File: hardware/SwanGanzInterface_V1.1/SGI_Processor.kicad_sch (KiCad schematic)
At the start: 29 parts, among them J2 Conn_01x08_Pin, SW2 MODE, SW3 ENTER, SW4 MODE, U4 XM0G3507QPTRQ1, U5 AdaFruit_1590, Y1 ABM8AIG-40.000MHZ-12-2Z-T3

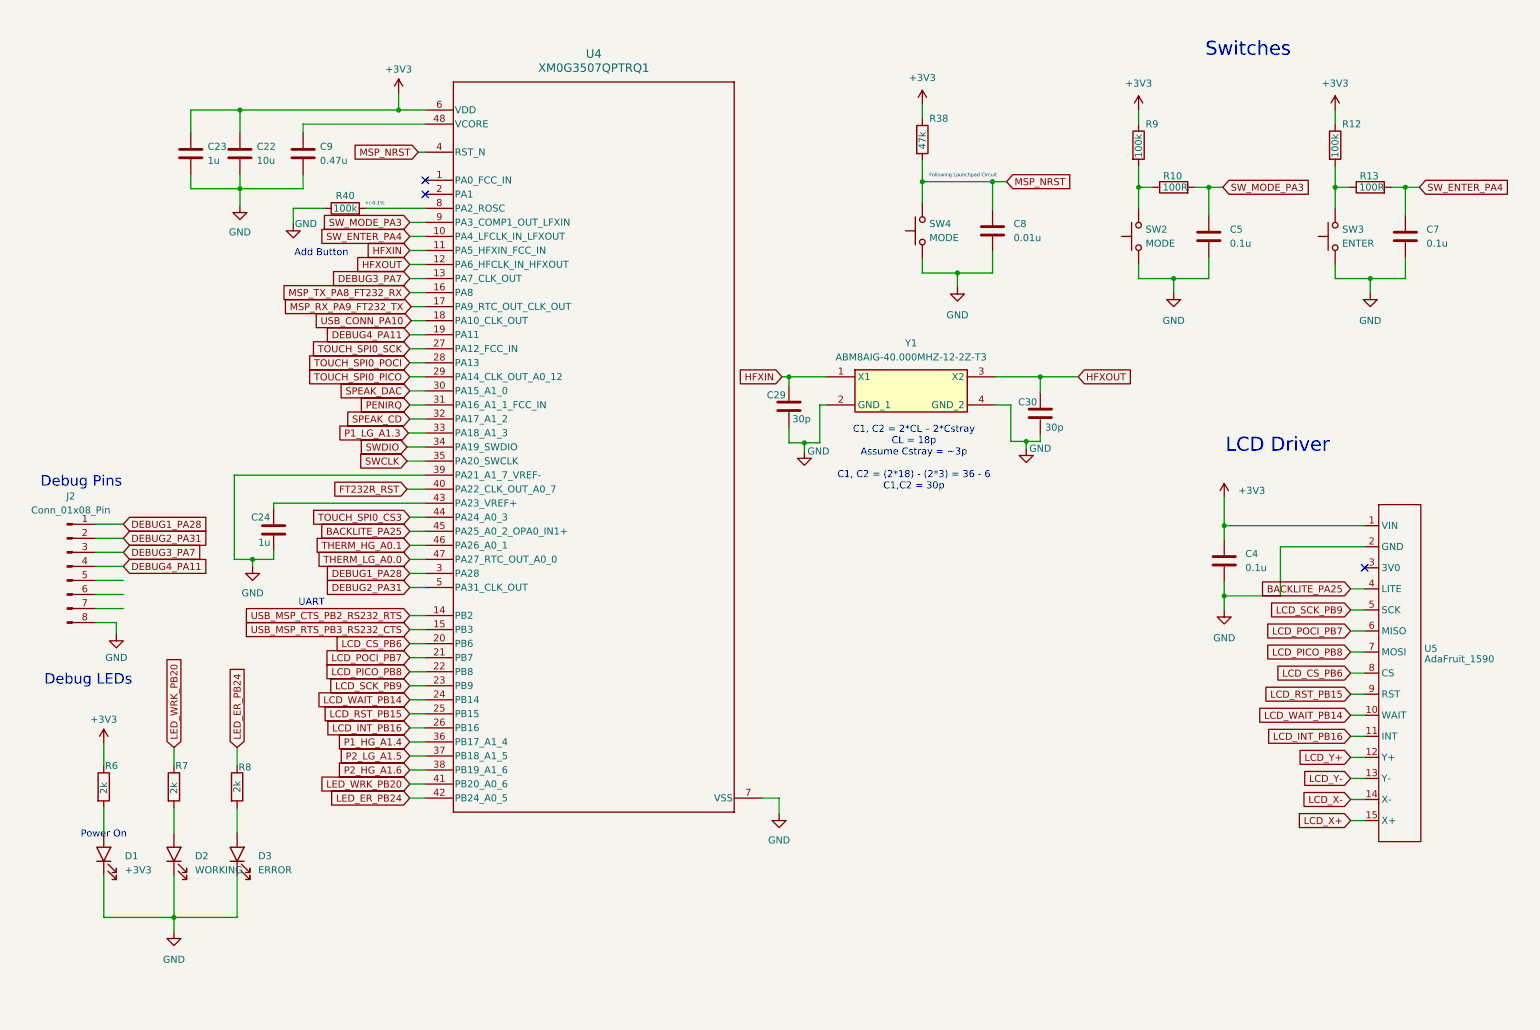
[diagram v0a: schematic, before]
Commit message: Got 64 pin MSP symbol and footprint and started implementation
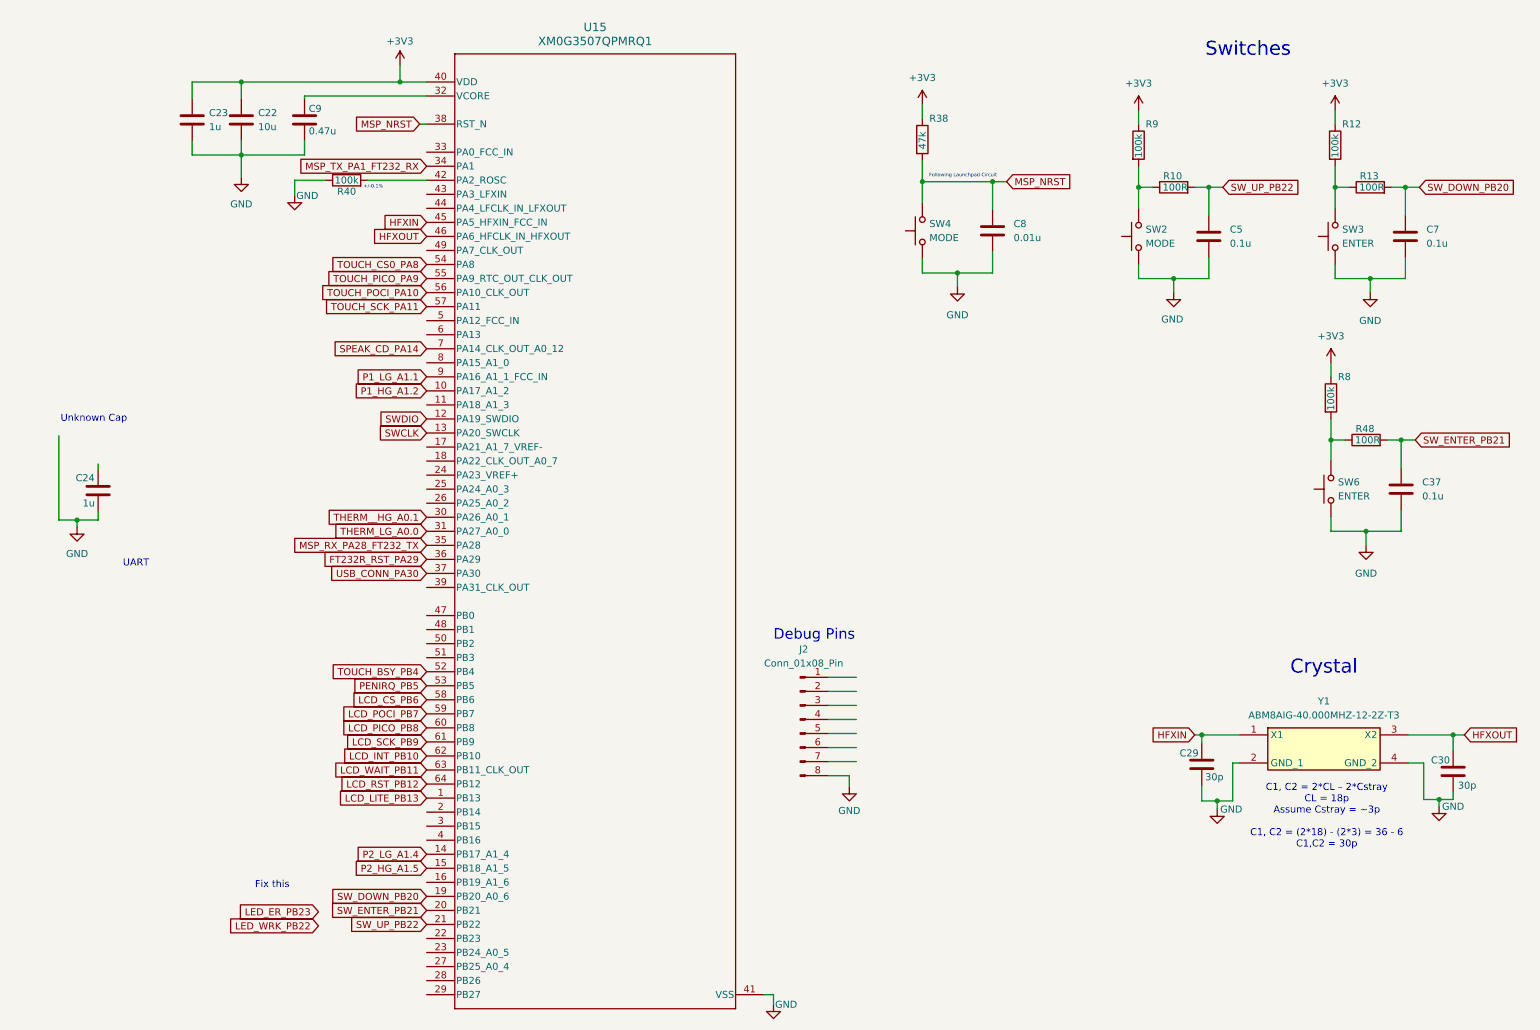
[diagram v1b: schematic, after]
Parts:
- removed C4: 0.1u, Capacitor_SMD:C_0603_1608Metric, symbol Device:C
- removed D1: +3V3, SGI_FootprintsLib:LED_D5.0mm, symbol SGI_SymbolLib:LED
- removed D2: WORKING, SGI_FootprintsLib:LED_D5.0mm, symbol SGI_SymbolLib:LED
- removed D3: ERROR, SGI_FootprintsLib:LED_D5.0mm, symbol SGI_SymbolLib:LED
- removed R6, R7: 2k, Resistor_SMD:R_0603_1608Metric, symbol Device:R
- removed U4: XM0G3507QPTRQ1, SGI_FootprintsLib:MSPM0_PT0048A-IPC_A, symbol SGI_SymbolLib:XM0G3507QPTRQ1
- removed U5: AdaFruit_1590, SGI_FootprintsLib:AdaFruit_1590, symbol SGI_SymbolLib:ADAFRUIT_1590_RA8875
- added C37: 0.1u, Capacitor_SMD:C_0603_1608Metric, symbol Device:C
- added R48: 100R, Resistor_SMD:R_0603_1608Metric, symbol Device:R
- added SW6: ENTER, SGI_FootprintsLib:SW_PUSH_6mm, symbol SGI_SymbolLib:SW_Push
- added U15: XM0G3507QPMRQ1, SGI_FootprintsLib:PM0064A-IPC_A, symbol SGI_SymbolLib:XM0G3507QPMRQ1
- R8: value 2k -> 100k
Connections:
- net LED_ER_PB24 is gone; now on net +3V3: R8.1
- net +3V3: now also U15.40 (VDD)
- net GND: now also C37.2, SW6.1, U15.41 (VSS)
- net HFXIN: now also U15.45 (PA5_HFXIN_FCC_IN)
- net HFXOUT: now also U15.46 (PA6_HFCLK_IN_HFXOUT)
- net LCD_CS_PB6: now also U15.58 (PB6)
- net LCD_PICO_PB8: now also U15.60 (PB8)
- net LCD_POCI_PB7: now also U15.59 (PB7)
- net LCD_SCK_PB9: now also U15.61 (PB9)
- net MSP_NRST: now also U15.38 (RST_N)
- net SWCLK: now also U15.13 (PA20_SWCLK)
- net SWDIO: now also U15.12 (PA19_SWDIO)
- net THERM_LG_A0.0: now also U15.31 (PA27_A0_0)
- net at C9.1: now also U15.32 (VCORE)
- net at R40.2: now also U15.42 (PA2_ROSC)
- net at R8.2: now also R48.1, SW6.2
- net DEBUG1_PA28: no longer names the net of J2.1 (Pin_1)
- net DEBUG2_PA31: no longer names the net of J2.2 (Pin_2)
- net DEBUG3_PA7: no longer names the net of J2.3 (Pin_3)
- net DEBUG4_PA11: no longer names the net of J2.4 (Pin_4)
- net SW_ENTER_PA4 renamed SW_DOWN_PB20
- net SW_DOWN_PB20: now also U15.19 (PB20_A0_6)
- net SW_MODE_PA3 renamed SW_UP_PB22
- net SW_UP_PB22: now also U15.21 (PB22)
- new net FT232R_RST_PA29: U15.36 (PA29)
- new net LCD_INT_PB10: U15.62 (PB10)
- new net LCD_LITE_PB13: U15.1 (PB13)
- new net LCD_RST_PB12: U15.64 (PB12)
- new net LCD_WAIT_PB11: U15.63 (PB11_CLK_OUT)
- new net MSP_RX_PA28_FT232_TX: U15.35 (PA28)
- new net MSP_TX_PA1_FT232_RX: U15.34 (PA1)
- new net P1_HG_A1.2: U15.10 (PA17_A1_2)
- new net P1_LG_A1.1: U15.9 (PA16_A1_1_FCC_IN)
- new net P2_HG_A1.5: U15.15 (PB18_A1_5)
- new net P2_LG_A1.4: U15.14 (PB17_A1_4)
- new net PENIRQ_PB5: U15.53 (PB5)
- new net SPEAK_CD_PA14: U15.7 (PA14_CLK_OUT_A0_12)
- new net SW_ENTER_PB21: C37.1, R48.2, U15.20 (PB21)
- new net THERM__HG_A0.1: U15.30 (PA26_A0_1)
- new net TOUCH_BSY_PB4: U15.52 (PB4)
- new net TOUCH_CS0_PA8: U15.54 (PA8)
- new net TOUCH_PICO_PA9: U15.55 (PA9_RTC_OUT_CLK_OUT)
- new net TOUCH_POCI_PA10: U15.56 (PA10_CLK_OUT)
- new net TOUCH_SCK_PA11: U15.57 (PA11)
- new net USB_CONN_PA30: U15.37 (PA30)
- no-connect marks 3 -> 0
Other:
- note added: "Crystal"
- note added: "Fix this"
- note added: "Unknown Cap"
- note removed: "Add Button"
- note removed: "Debug LEDs"
- note removed: "LCD Driver"
- note removed: "Power On"
- moved on the sheet: C22, C23, C24, C29, C30, C9, J2, R40, Y1

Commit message: Added debug pins to touch ic and ft232
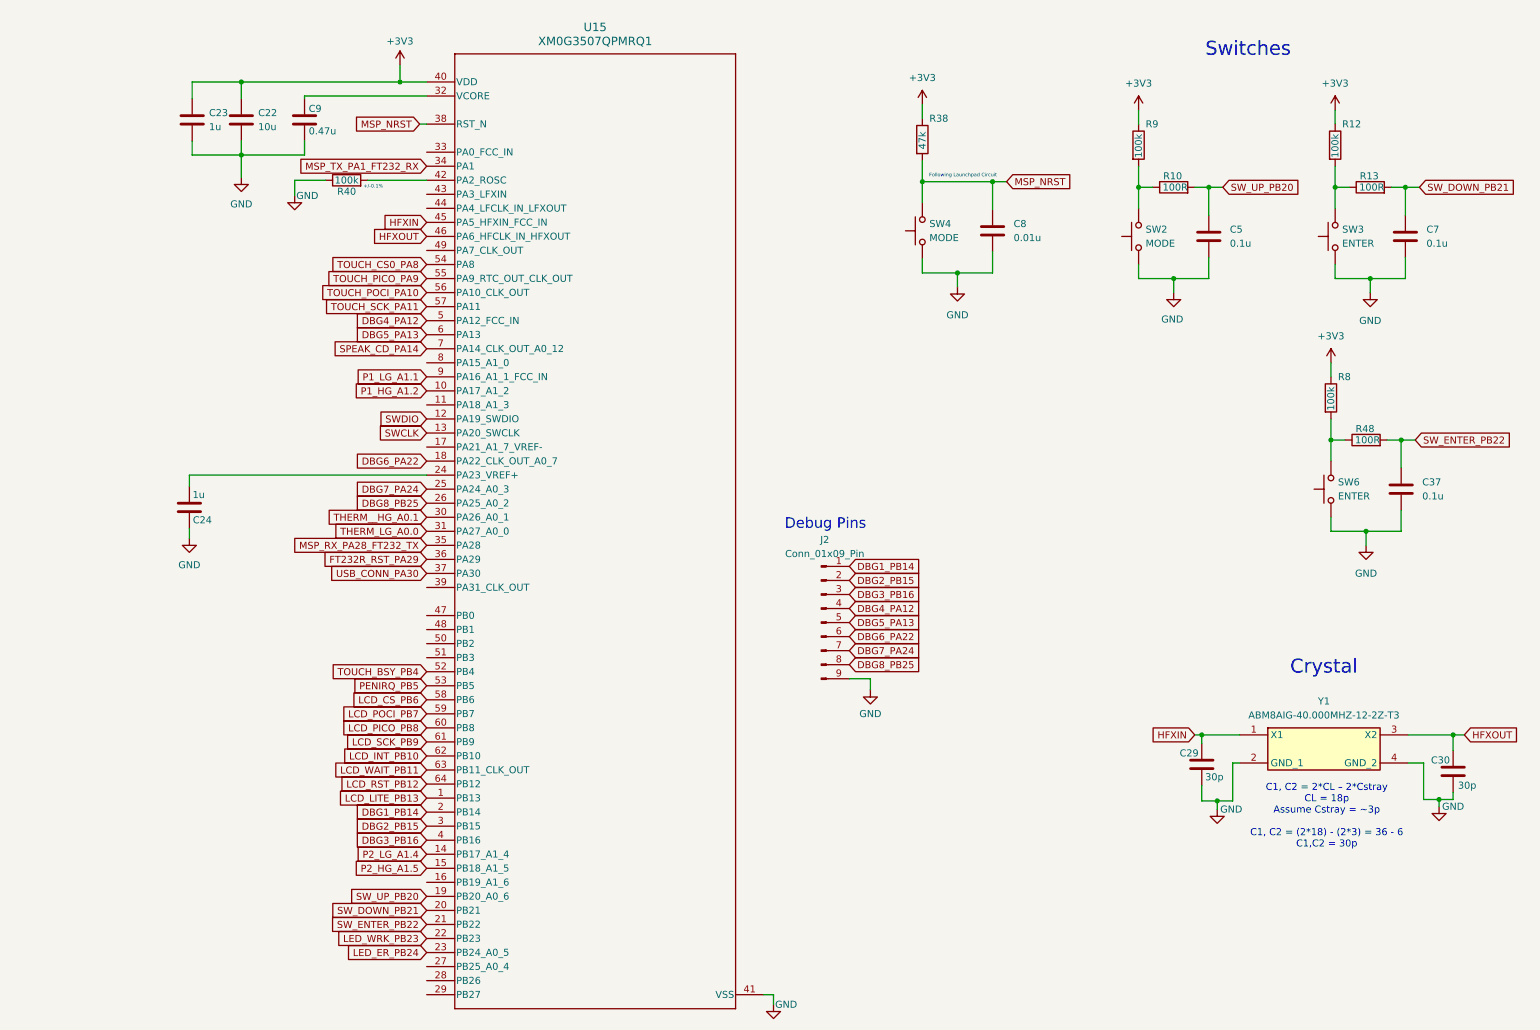
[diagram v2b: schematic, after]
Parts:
- removed J2: Conn_01x08_Pin, Connector_PinHeader_2.54mm:PinHeader_1x08_P2.54mm_Vertical, symbol Connector:Conn_01x08_Pin
- added J2: Conn_01x09_Pin, Connector_PinSocket_2.54mm:PinSocket_1x09_P2.54mm_Vertical, symbol Connector:Conn_01x09_Pin
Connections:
- net GND: now also C24.1, J2.9 (Pin_9); no longer C24.2
- net DBG6_PA22: now reaches U15.18 (PA22_CLK_OUT_A0_7)
- net DBG6_PA22: now also J2.6 (Pin_6)
- net DBG1_PB14: now reaches U15.2 (PB14)
- net DBG1_PB14: now also J2.1 (Pin_1)
- net LED_WRK_PB23: now reaches U15.22 (PB23)
- net LED_ER_PB24: now reaches U15.23 (PB24_A0_5)
- net at U15.24 (PA23_VREF+): now also C24.2
- net DBG7_PA24: now reaches U15.25 (PA24_A0_3)
- net DBG7_PA24: now also J2.7 (Pin_7)
- net DBG8_PB25: now reaches U15.26 (PA25_A0_2)
- net DBG8_PB25: now also J2.8 (Pin_8)
- net DBG2_PB15: now reaches U15.3 (PB15)
- net DBG2_PB15: now also J2.2 (Pin_2)
- net DBG3_PB16: now reaches U15.4 (PB16)
- net DBG3_PB16: now also J2.3 (Pin_3)
- net DBG4_PA12: now reaches U15.5 (PA12_FCC_IN)
- net DBG4_PA12: now also J2.4 (Pin_4)
- net DBG5_PA13: now reaches U15.6 (PA13)
- net DBG5_PA13: now also J2.5 (Pin_5)
- net SW_DOWN_PB20 renamed SW_DOWN_PB21
- net SW_DOWN_PB21: now also U15.20 (PB21); no longer U15.19 (PB20_A0_6)
- net SW_ENTER_PB21 renamed SW_ENTER_PB22
- net SW_ENTER_PB22: now also U15.21 (PB22); no longer U15.20 (PB21)
- net SW_UP_PB22 renamed SW_UP_PB20
- net SW_UP_PB20: now also U15.19 (PB20_A0_6); no longer U15.21 (PB22)
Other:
- note removed: "Fix this"
- note removed: "UART"
- note removed: "Unknown Cap"
- moved on the sheet: C24

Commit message: Schematic Check
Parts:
- added J14: Conn_01x03_Pin, Connector_PinHeader_2.54mm:PinHeader_1x03_P2.54mm_Vertical, symbol Connector:Conn_01x03_Pin
- renumbered C29 to C10, C5 to C11, C37 to C12, C7 to C13, C30 to C14, C24 to C5, C23 to C6, C22 to C7, C9 to C8, C8 to C9, R48 to R10, R13 to R11, R40 to R4, R38 to R5, R9 to R6, R10 to R7, R12 to R9, SW4 to SW2, SW2 to SW3, SW6 to SW4, SW3 to SW5, U15 to U4
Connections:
- net GND: now also U4.17 (PA21_A1_7_VREF-), J14.3 (Pin_3)
- net MSP_RTS_PB25_FT_CTS: now reaches U4.27 (PB25_A0_4)
- net MSP_CTS_PB26_FT_RTS: now reaches U4.28 (PB26)
- net SPEAK_DAC_PA15: now reaches U4.8 (PA15_A1_0)
- net FT232R_RST_PA29 renamed FT_RST_PA29
- net MSP_RX_PA28_FT232_TX renamed MSP_TX_PA28_FT_RX
- net MSP_TX_PA1_FT232_RX renamed MSP_RX_PA1_FT_TX
- net SWCLK renamed SWCLK_PA20
- net SWCLK_PA20: now also J14.2 (Pin_2)
- net SWDIO renamed SWDIO_PA19
- net SWDIO_PA19: now also J14.1 (Pin_1)
- no-connect marks 0 -> 12
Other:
- note added: "MSPM0 Reset"
- note added: "Processor"
- note added: "Programming Pins"
- moved on the sheet: C5, C6, C7, C8, J2, R4, U4

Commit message: Filter paramaters and assigned footprints
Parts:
- C10, C14, C5, C6: footprint (none) -> Capacitor_SMD:C_0603_1608Metric
- C7: footprint (none) -> Capacitor_SMD:C_1206_3216Metric
- C8: footprint (none) -> Capacitor_SMD:C_0603_1608Metric_Pad1.08x0.95mm_HandSolder
- R4: footprint (none) -> Resistor_SMD:R_0603_1608Metric
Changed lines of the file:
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@@
 			)
 		)
-		(property "Footprint" ""
+		(property "Footprint" "Capacitor_SMD:C_0603_1608Metric"
 			(at 225.6028 145.034 0)
 			(effects
@@
 			)
 		)
-		(property "Footprint" ""
+		(property "Footprint" "Capacitor_SMD:C_0603_1608Metric_Pad1.08x0.95mm_HandSolder"
 			(at 79.1972 35.814 0)
 			(effects
@@
 			)
 		)
-		(property "Footprint" ""
+		(property "Footprint" "Capacitor_SMD:C_1206_3216Metric"
 			(at 67.7672 35.814 0)
 			(effects
@@
 			)
 		)
-		(property "Footprint" ""
+		(property "Footprint" "Resistor_SMD:R_0603_1608Metric"
 			(at 85.852 44.704 90)
 			(effects
@@
 			)
 		)
-		(property "Footprint" ""
+		(property "Footprint" "Capacitor_SMD:C_0603_1608Metric"
 			(at 271.0688 146.304 0)
 			(effects
@@
 			)
 		)
-		(property "Footprint" ""
+		(property "Footprint" "Capacitor_SMD:C_0603_1608Metric"
 			(at 56.4388 98.298 0)
 			(effects
@@
 			)
 		)
-		(property "Footprint" ""
+		(property "Footprint" "Capacitor_SMD:C_0603_1608Metric"
 			(at 58.8772 35.814 0)
 			(effects

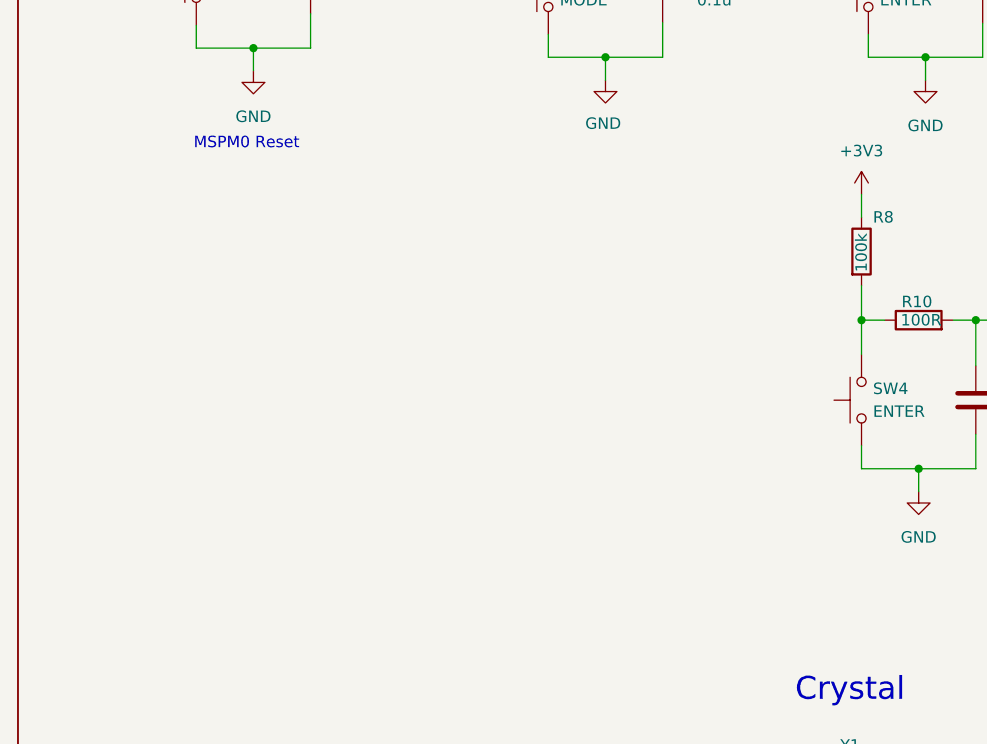
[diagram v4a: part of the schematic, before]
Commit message: Block Diagram for Layout
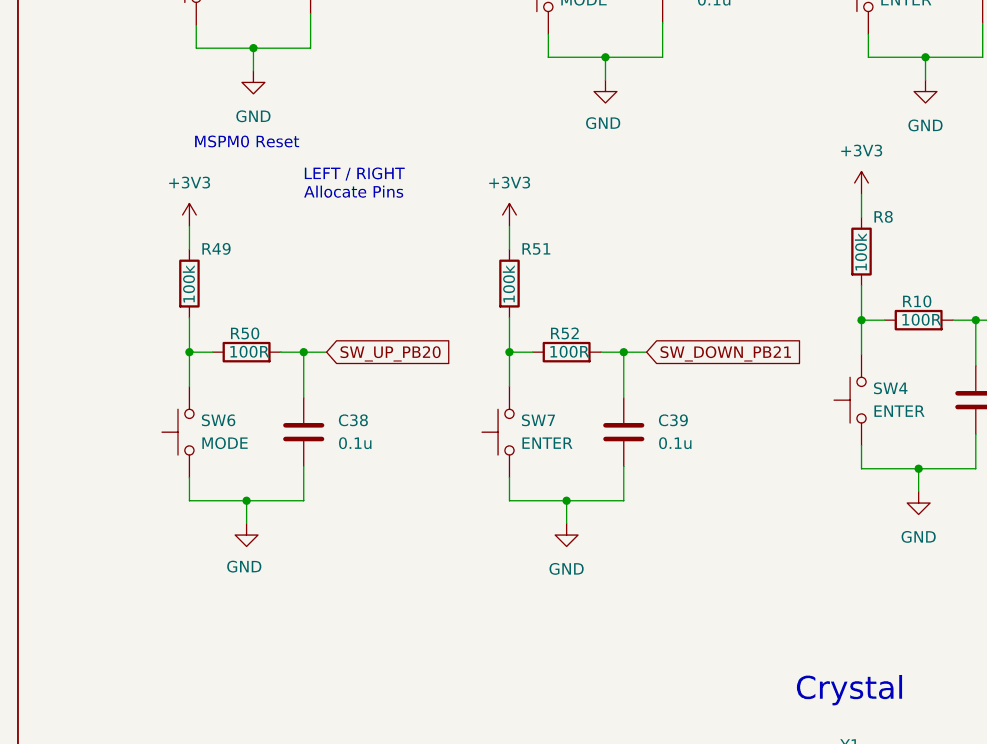
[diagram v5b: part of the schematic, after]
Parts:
- added C38, C39: 0.1u, Capacitor_SMD:C_0603_1608Metric, symbol Device:C
- added R49, R51: 100k, Resistor_SMD:R_0603_1608Metric, symbol Device:R
- added R50, R52: 100R, Resistor_SMD:R_0603_1608Metric, symbol Device:R
- added SW6: MODE, SGI_FootprintsLib:SW_PUSH_6mm, symbol SGI_SymbolLib:SW_Push
- added SW7: ENTER, SGI_FootprintsLib:SW_PUSH_6mm, symbol SGI_SymbolLib:SW_Push
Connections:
- net +3V3: now also R49.1, R51.1
- net GND: now also C38.2, C39.2, SW6.1, SW7.1
- net SW_DOWN_PB21: now also C39.1, R52.2
- net SW_UP_PB20: now also C38.1, R50.2
- new net: R51.2, R52.1, SW7.2
- new net: R49.2, R50.1, SW6.2
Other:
- note added: "LEFT / RIGHT Allocate Pins"

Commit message: Layout work on screen and expanded board size
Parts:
- SW2: value MODE -> NRST
- SW3: value MODE -> UP
- SW5: value ENTER -> DOWN
- SW6: value MODE -> LEFT
- SW7: value ENTER -> RIGHT
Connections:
- net SW_UP_PB20: no longer C38.1, R50.2
- new net SW_LEFT_PB20: C38.1, R50.2
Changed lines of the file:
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@@
 		)
 	)
-	(global_label "SW_UP_PB20"
+	(global_label "SW_LEFT_PB20"
 		(shape input)
 		(at 190.5 93.726 0)
@@
 		)
 		(property "Intersheetrefs" "${INTERSHEET_REFS}"
-			(at 205.6408 93.726 0)
+			(at 207.2736 93.726 0)
 			(effects
 				(font
@@
 		(fields_autoplaced yes)
 		(property "Reference" "SW3"
-			(at 216.408 52.0699 90)
+			(at 217.17 52.0699 90)
 			(effects
 				(font
@@
 			)
 		)
-		(property "Value" "MODE"
-			(at 216.408 54.6099 90)
+		(property "Value" "UP"
+			(at 217.17 54.6099 90)
 			(effects
 				(font
@@
 		(fields_autoplaced yes)
 		(property "Reference" "SW2"
-			(at 177.292 51.0539 90)
+			(at 177.8 51.0539 90)
 			(effects
 				(font
@@
 			)
 		)
-		(property "Value" "MODE"
-			(at 177.292 53.5939 90)
+		(property "Value" "NRST"
+			(at 177.8 53.5939 90)
 			(effects
 				(font
@@
 			)
 		)
-		(property "Value" "ENTER"
+		(property "Value" "RIGHT"
 			(at 212.09 103.8859 90)
 			(effects
@@
 		(fields_autoplaced yes)
 		(property "Reference" "SW5"
-			(at 251.968 52.0699 90)
+			(at 252.73 52.0699 90)
 			(effects
 				(font
@@
 			)
 		)
-		(property "Value" "ENTER"
-			(at 251.968 54.6099 90)
+		(property "Value" "DOWN"
+			(at 252.73 54.6099 90)
 			(effects
 				(font
@@
 			)
 		)
-		(property "Value" "MODE"
+		(property "Value" "LEFT"
 			(at 176.53 103.8859 90)
 			(effects
